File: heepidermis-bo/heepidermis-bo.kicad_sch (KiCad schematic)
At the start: 1 part

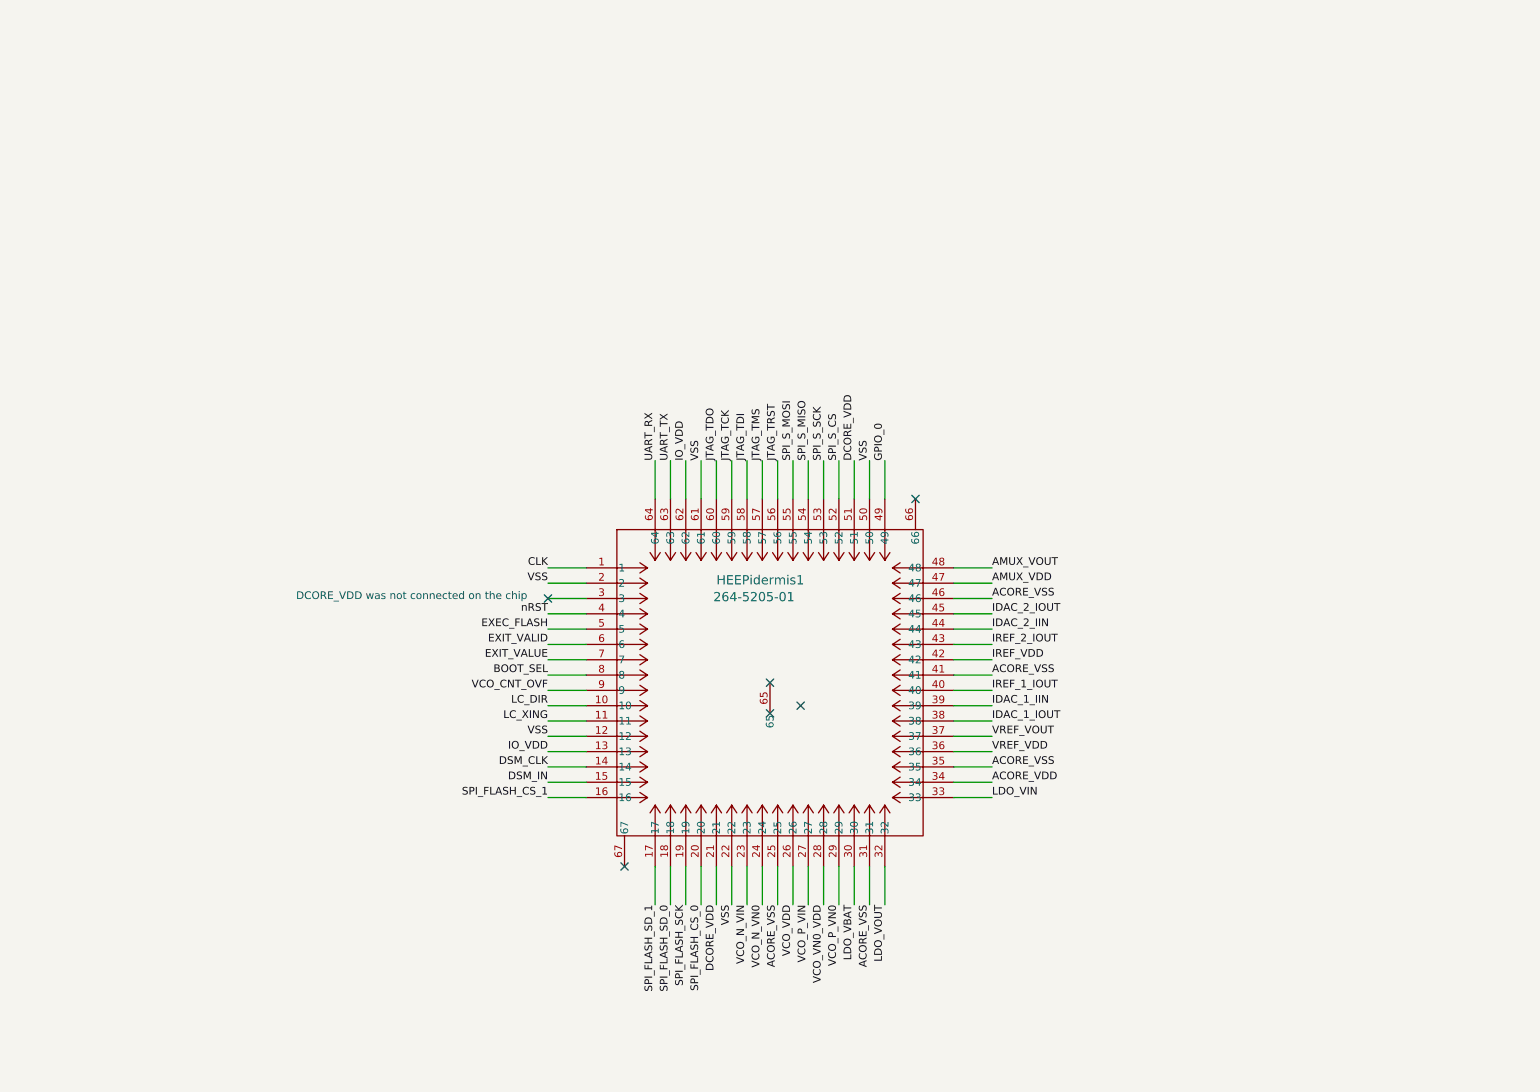
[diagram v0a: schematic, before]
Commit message: Previous to changing connector to 2.54
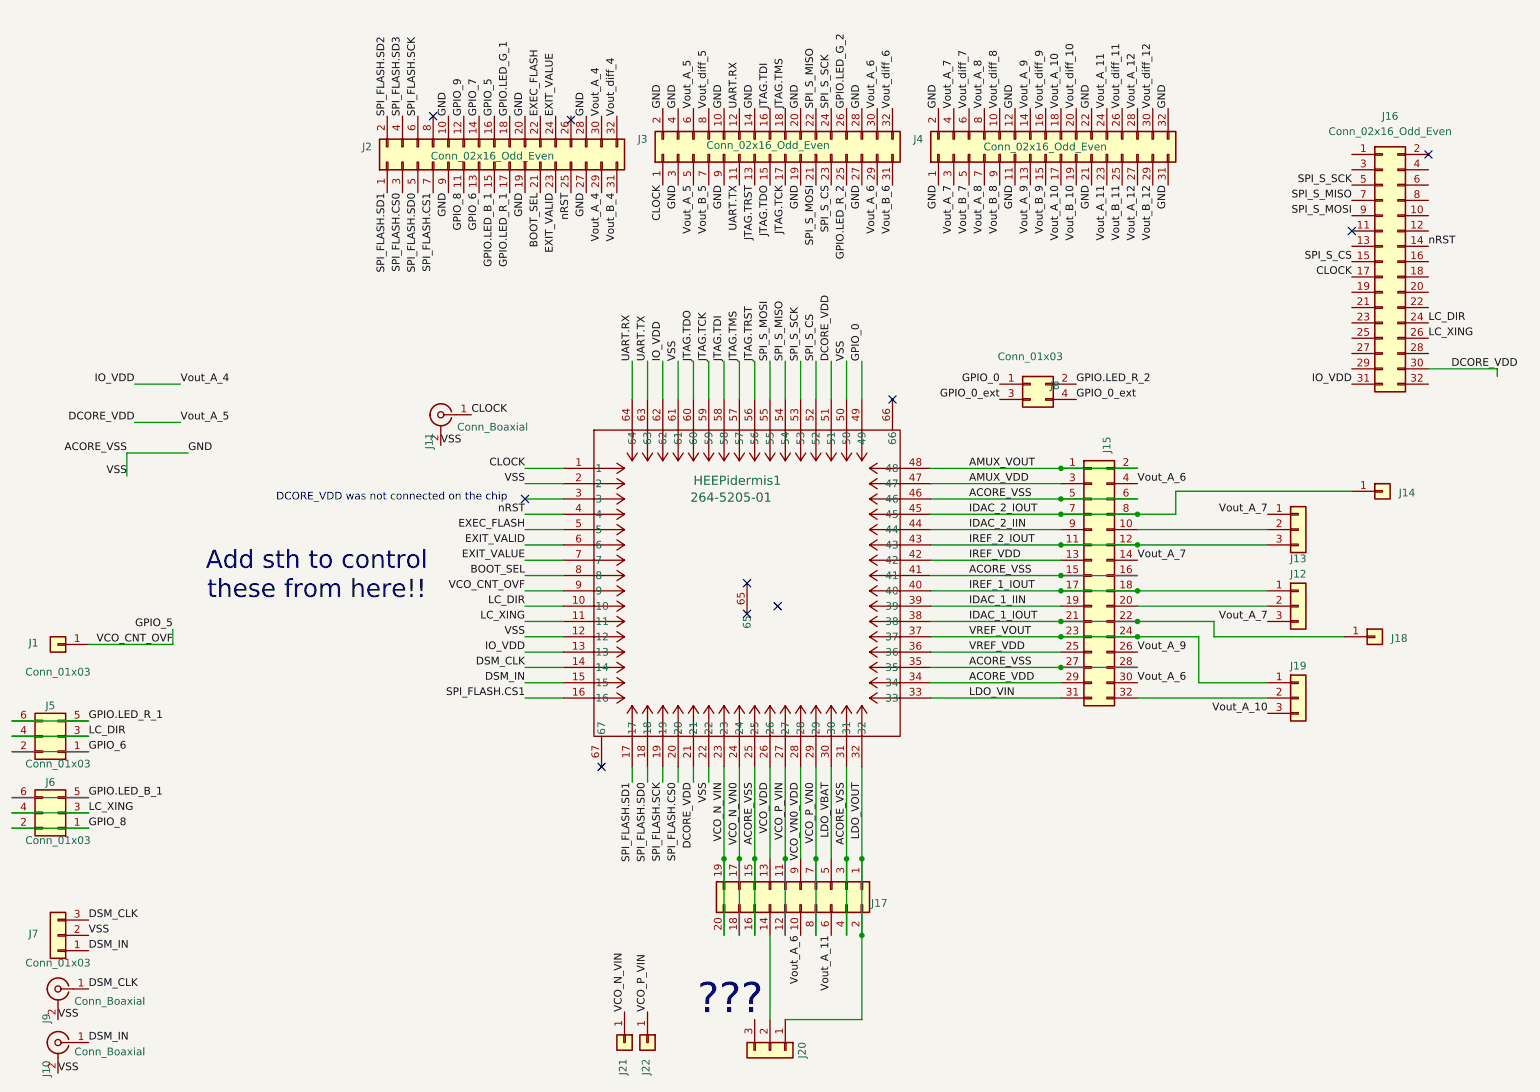
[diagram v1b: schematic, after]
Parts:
- added J1, J14, J18, J21, J22: Conn_01x03, Connector_PinHeader_1.27mm:PinHeader_1x01_P1.27mm_Vertical, symbol Connector_Generic:Conn_01x01
- added J10, J11, J9: Conn_Boaxial, Connector_Coaxial:SMA_Amphenol_901-144_Vertical, symbol Connector:Conn_Coaxial
- added J12, J13, J19, J20, J7: Conn_01x03, Connector_PinHeader_2.54mm:PinHeader_1x03_P2.54mm_Vertical, symbol Connector_Generic:Conn_01x03
- added J15: Conn_02x16_Odd_Even, Connector_PinHeader_2.54mm:PinHeader_1x16_P2.54mm_Vertical, symbol Connector_Generic:Conn_02x16_Odd_Even
- added J16, J2, J3, J4: Conn_02x16_Odd_Even, symbol Connector_Generic:Conn_02x16_Odd_Even
- added J17: Conn_02x10_Odd_Even, Connector_PinHeader_2.54mm:PinHeader_2x10_P2.54mm_Vertical, symbol Connector_Generic:Conn_02x10_Odd_Even
- added J5, J6: Conn_01x03, Connector_PinHeader_1.27mm:PinHeader_2x03_P1.27mm_Vertical, symbol Connector_Generic:Conn_02x03_Odd_Even
- added J8: Conn_01x03, Connector_PinHeader_1.27mm:PinHeader_2x02_P1.27mm_Vertical, symbol Connector_Generic:Conn_02x02_Odd_Even
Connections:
- net VSS is gone; now on net ACORE_VSS: HEEPidermis1.12, HEEPidermis1.2, HEEPidermis1.22, HEEPidermis1.50, HEEPidermis1.61
- net ACORE_VDD: now also J15.29 (Pin_29)
- net ACORE_VSS: now also J10.2 (Ext), J11.2 (Ext), J15.15 (Pin_15), J15.16 (Pin_16), J15.27 (Pin_27), J15.28 (Pin_28), J15.5 (Pin_5), J15.6 (Pin_6), J17.15 (Pin_15), J17.16 (Pin_16), J17.3 (Pin_3), J17.4 (Pin_4), J2.10 (Pin_10), J2.19 (Pin_19), J2.20 (Pin_20), J2.27 (Pin_27), J2.28 (Pin_28), J2.9 (Pin_9), J3.10 (Pin_10), J3.14 (Pin_14), J3.19 (Pin_19), J3.2 (Pin_2), J3.20 (Pin_20), J3.27 (Pin_27), J3.28 (Pin_28), J3.3 (Pin_3), J3.4 (Pin_4), J3.9 (Pin_9), J4.1 (Pin_1), J4.11 (Pin_11), J4.12 (Pin_12), J4.2 (Pin_2), J4.21 (Pin_21), J4.22 (Pin_22), J4.31 (Pin_31), J4.32 (Pin_32), J7.2 (Pin_2), J9.2 (Ext)
- net AMUX_VDD: now also J15.3 (Pin_3)
- net AMUX_VOUT: now also J15.1 (Pin_1), J15.2 (Pin_2)
- net BOOT_SEL: now also J2.21 (Pin_21)
- net DCORE_VDD: now also J16.30 (Pin_30), J3.5 (Pin_5), J3.6 (Pin_6)
- net DSM_CLK: now also J7.3 (Pin_3), J9.1 (In)
- net DSM_IN: now also J10.1 (In), J7.1 (Pin_1)
- net EXEC_FLASH: now also J2.22 (Pin_22)
- net EXIT_VALID: now also J2.23 (Pin_23)
- net EXIT_VALUE: now also J2.24 (Pin_24)
- net GPIO_0: now also J8.1 (Pin_1)
- net IDAC_1_IIN: now also J15.19 (Pin_19)
- net IDAC_1_IOUT: now also J15.21 (Pin_21), J15.22 (Pin_22), J18.1 (Pin_1)
- net IDAC_2_IIN: now also J15.9 (Pin_9)
- net IDAC_2_IOUT: now also J14.1 (Pin_1), J15.7 (Pin_7), J15.8 (Pin_8)
- net IO_VDD: now also J16.31 (Pin_31), J2.29 (Pin_29), J2.30 (Pin_30)
- net IREF_1_IOUT: now also J12.1 (Pin_1), J15.17 (Pin_17), J15.18 (Pin_18)
- net IREF_2_IOUT: now also J13.3 (Pin_3), J15.11 (Pin_11), J15.12 (Pin_12)
- net IREF_VDD: now also J15.13 (Pin_13)
- net LC_DIR: now also J16.24 (Pin_24), J5.3 (Pin_3), J5.4 (Pin_4)
- net LC_XING: now also J16.26 (Pin_26), J6.3 (Pin_3), J6.4 (Pin_4)
- net LDO_VBAT: now also J17.5 (Pin_5)
- net LDO_VIN: now also J15.31 (Pin_31)
- net LDO_VOUT: now also J17.1 (Pin_1), J17.2 (Pin_2), J20.1 (Pin_1)
- net SPI_S_CS: now also J16.15 (Pin_15), J3.23 (Pin_23)
- net SPI_S_MISO: now also J16.7 (Pin_7), J3.22 (Pin_22)
- net SPI_S_MOSI: now also J16.9 (Pin_9), J3.21 (Pin_21)
- net SPI_S_SCK: now also J16.5 (Pin_5), J3.24 (Pin_24)
- net VCO_N_VIN: now also J17.19 (Pin_19), J17.20 (Pin_20), J21.1 (Pin_1)
- net VCO_N_VN0: now also J17.17 (Pin_17), J17.18 (Pin_18)
- net VCO_P_VIN: now also J17.11 (Pin_11), J17.12 (Pin_12), J22.1 (Pin_1)
- net VCO_P_VN0: now also J17.7 (Pin_7), J17.8 (Pin_8)
- net VCO_VDD: now also J17.13 (Pin_13)
- net VCO_VN0_VDD: now also J17.9 (Pin_9)
- net VREF_VDD: now also J15.25 (Pin_25)
- net VREF_VOUT: now also J15.23 (Pin_23), J15.24 (Pin_24), J19.1 (Pin_1)
- net nRST: now also J16.14 (Pin_14), J2.25 (Pin_25)
- net CLK renamed CLOCK
- net CLOCK: now also J11.1 (In), J16.17 (Pin_17), J3.1 (Pin_1)
- net JTAG_TCK renamed JTAG.TCK
- net JTAG.TCK: now also J3.17 (Pin_17)
- net JTAG_TDI renamed JTAG.TDI
- net JTAG.TDI: now also J3.16 (Pin_16)
- net JTAG_TDO renamed JTAG.TDO
- net JTAG.TDO: now also J3.15 (Pin_15)
- net JTAG_TMS renamed JTAG.TMS
- net JTAG.TMS: now also J3.18 (Pin_18)
- net JTAG_TRST renamed JTAG.TRST
- net JTAG.TRST: now also J3.13 (Pin_13)
- net SPI_FLASH_CS_0 renamed SPI_FLASH.CS0
- net SPI_FLASH.CS0: now also J2.3 (Pin_3)
- net SPI_FLASH_CS_1 renamed SPI_FLASH.CS1
- net SPI_FLASH.CS1: now also J2.7 (Pin_7)
- net SPI_FLASH_SCK renamed SPI_FLASH.SCK
- net SPI_FLASH.SCK: now also J2.6 (Pin_6)
- net SPI_FLASH_SD_0 renamed SPI_FLASH.SD0
- net SPI_FLASH.SD0: now also J2.5 (Pin_5)
- net SPI_FLASH_SD_1 renamed SPI_FLASH.SD1
- net SPI_FLASH.SD1: now also J2.1 (Pin_1)
- net UART_RX renamed UART.RX
- net UART.RX: now also J3.12 (Pin_12)
- net UART_TX renamed UART.TX
- net UART.TX: now also J3.11 (Pin_11)
- net VCO_CNT_OVF renamed GPIO_5
- net GPIO_5: now also J1.1 (Pin_1), J2.16 (Pin_16)
- new net: J17.14 (Pin_14), J20.2 (Pin_2)
- new net: J13.2 (Pin_2), J15.10 (Pin_10)
- new net: J12.2 (Pin_2), J15.20 (Pin_20)
- new net: J15.32 (Pin_32), J19.2 (Pin_2)
- new net GPIO.LED_B_1: J2.15 (Pin_15), J6.5 (Pin_5), J6.6 (Pin_6)
- new net GPIO.LED_G_1: J2.18 (Pin_18)
- new net GPIO.LED_G_2: J3.26 (Pin_26)
- new net GPIO.LED_R_1: J2.17 (Pin_17), J5.5 (Pin_5), J5.6 (Pin_6)
- new net GPIO.LED_R_2: J3.25 (Pin_25), J8.2 (Pin_2)
- new net GPIO_0_ext: J8.3 (Pin_3), J8.4 (Pin_4)
- new net GPIO_6: J2.13 (Pin_13), J5.1 (Pin_1), J5.2 (Pin_2)
- new net GPIO_7: J2.14 (Pin_14)
- new net GPIO_8: J2.11 (Pin_11), J6.1 (Pin_1), J6.2 (Pin_2)
- new net GPIO_9: J2.12 (Pin_12)
- new net SPI_FLASH.SD2: J2.2 (Pin_2)
- new net SPI_FLASH.SD3: J2.4 (Pin_4)
- new net Vout_A_10: J19.3 (Pin_3), J4.17 (Pin_17), J4.18 (Pin_18)
- new net Vout_A_11: J17.6 (Pin_6), J4.23 (Pin_23), J4.24 (Pin_24)
- new net Vout_A_12: J4.27 (Pin_27), J4.28 (Pin_28)
- new net Vout_A_6: J15.30 (Pin_30), J15.4 (Pin_4), J17.10 (Pin_10), J3.29 (Pin_29), J3.30 (Pin_30)
- new net Vout_A_7: J12.3 (Pin_3), J13.1 (Pin_1), J15.14 (Pin_14), J4.3 (Pin_3), J4.4 (Pin_4)
- new net Vout_A_8: J4.7 (Pin_7), J4.8 (Pin_8)
- new net Vout_A_9: J15.26 (Pin_26), J4.13 (Pin_13), J4.14 (Pin_14)
- new net Vout_B_10: J4.19 (Pin_19)
- new net Vout_B_11: J4.25 (Pin_25)
- new net Vout_B_12: J4.29 (Pin_29)
- new net Vout_B_4: J2.31 (Pin_31)
- new net Vout_B_5: J3.7 (Pin_7)
- new net Vout_B_6: J3.31 (Pin_31)
- new net Vout_B_7: J4.5 (Pin_5)
- new net Vout_B_8: J4.9 (Pin_9)
- new net Vout_B_9: J4.15 (Pin_15)
- new net Vout_diff_10: J4.20 (Pin_20)
- new net Vout_diff_11: J4.26 (Pin_26)
- new net Vout_diff_12: J4.30 (Pin_30)
- new net Vout_diff_4: J2.32 (Pin_32)
- new net Vout_diff_5: J3.8 (Pin_8)
- new net Vout_diff_6: J3.32 (Pin_32)
- new net Vout_diff_7: J4.6 (Pin_6)
- new net Vout_diff_8: J4.10 (Pin_10)
- new net Vout_diff_9: J4.16 (Pin_16)
- no-connect marks 6 -> 10
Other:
- note added: "???"
- note added: "Add sth to control these from here!!"
- moved on the sheet: HEEPidermis1
